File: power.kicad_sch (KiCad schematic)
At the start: 32 parts, among them J1 Barrel_Jack_MountingPin, J2 Conn_02x04_Odd_Even, J3 Conn_02x04_Odd_Even, Q1 SI2301CDS-T1-GE3, SW1 Power, U2 TPS54302

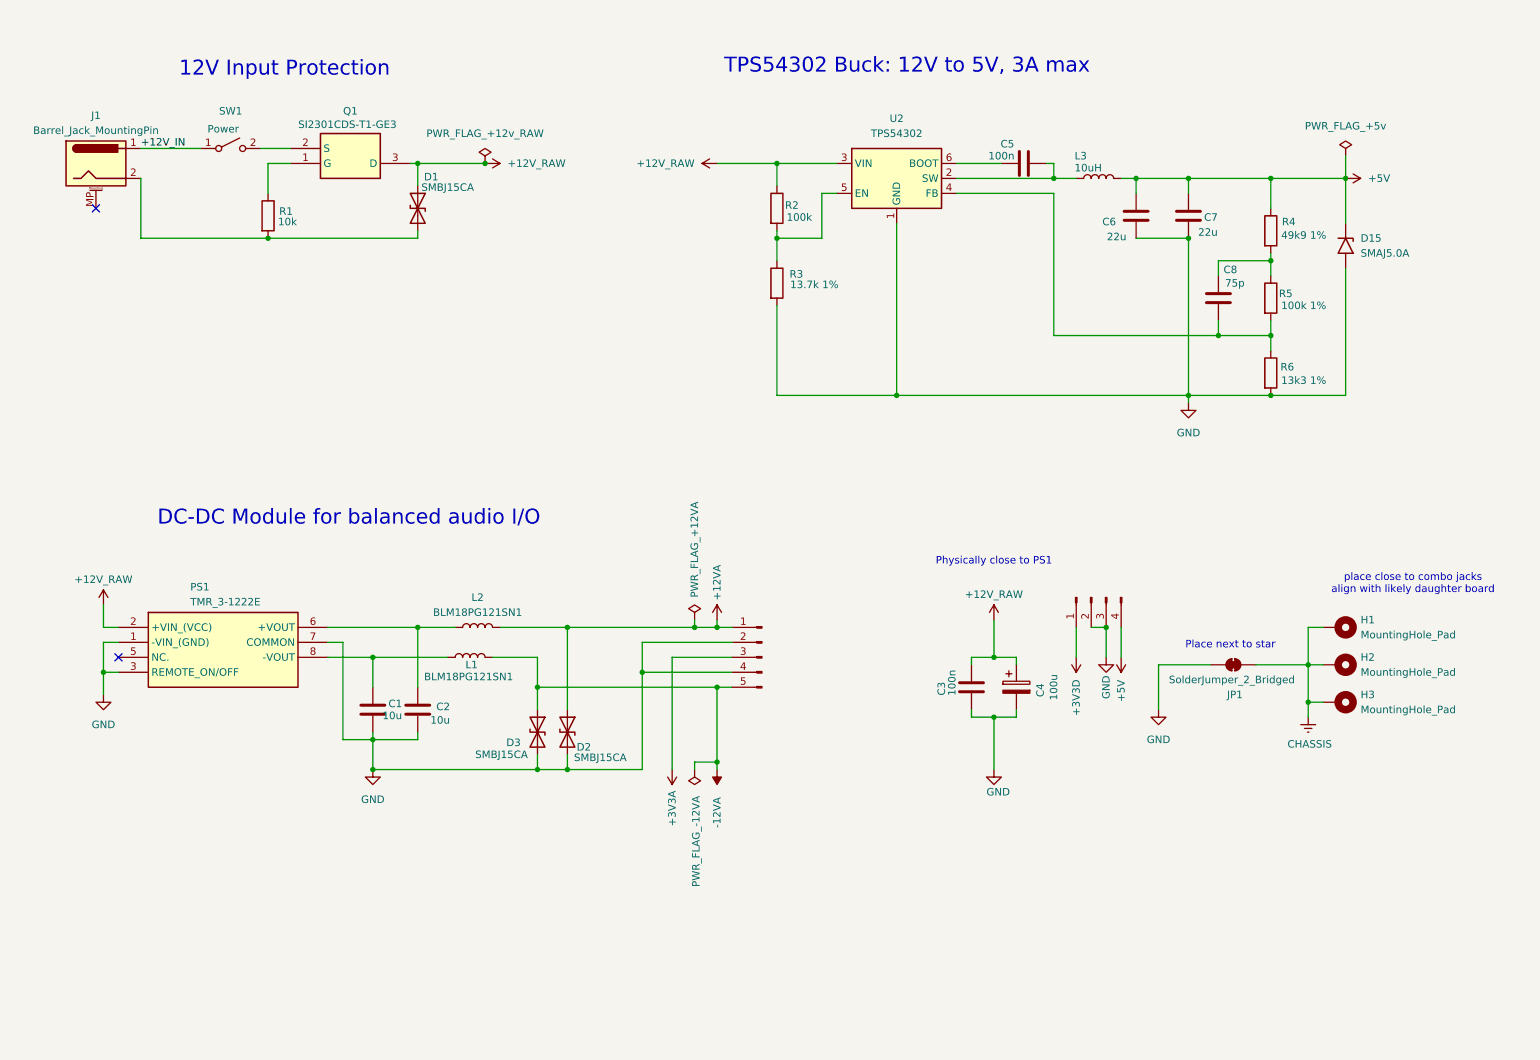
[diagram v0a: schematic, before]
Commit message: change docs to use RS3-1212D
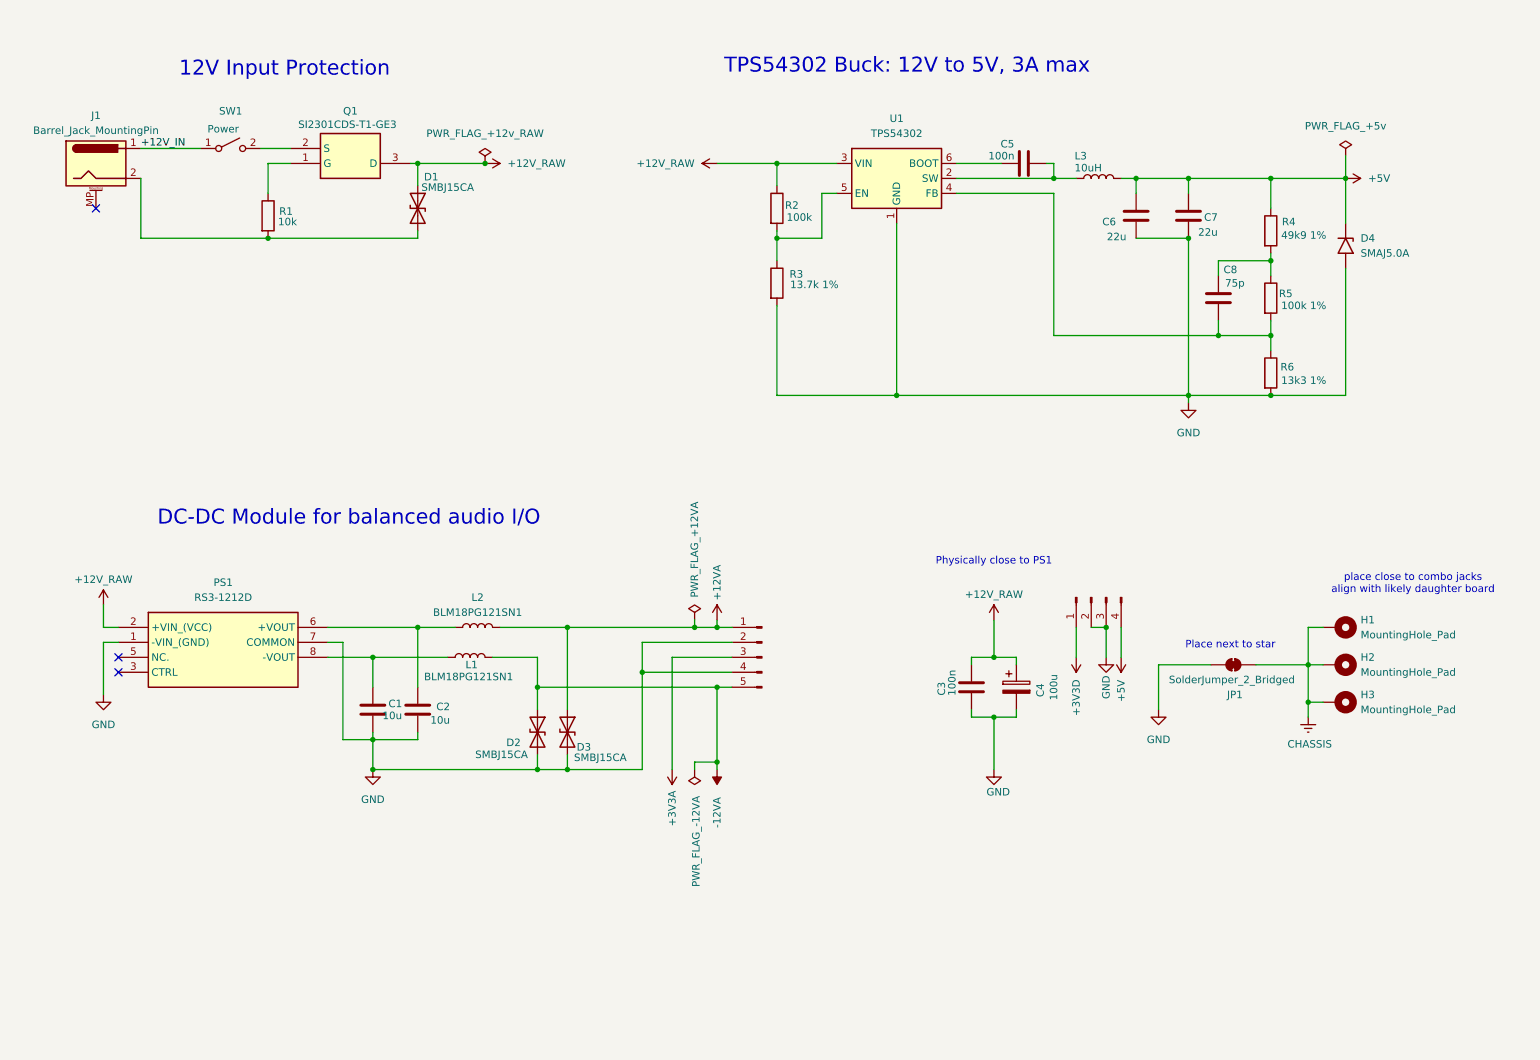
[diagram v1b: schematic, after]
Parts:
- removed PS1: TMR_3-1222E, daisy-studio:TMR1210, symbol daisy-studio:TMR_3-1222E
- added PS1: RS3-1212D, daisy-studio:TMR1210, symbol daisy-studio:RS3-1212D
- renumbered D3 to D2, D2 to D3, D15 to D4, U2 to U1
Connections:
- net +12V_RAW: now also PS1.2 (+VIN_(VCC))
- net GND: now also PS1.1 (-VIN_(GND)), PS1.7 (COMMON)
- net at C2.1, L2.1: now also PS1.6 (+VOUT)
- net at C1.1, L1.1: now also PS1.8 (-VOUT)
- no-connect marks 2 -> 3

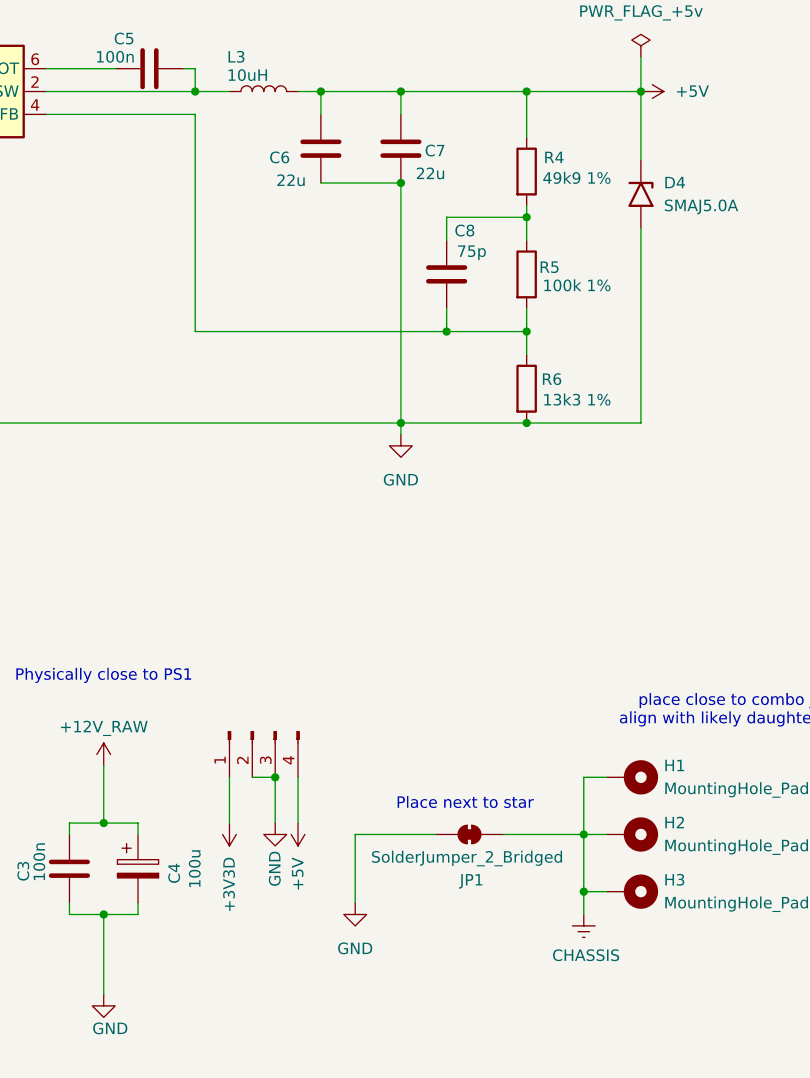
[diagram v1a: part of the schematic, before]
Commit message: clean up symbols and values
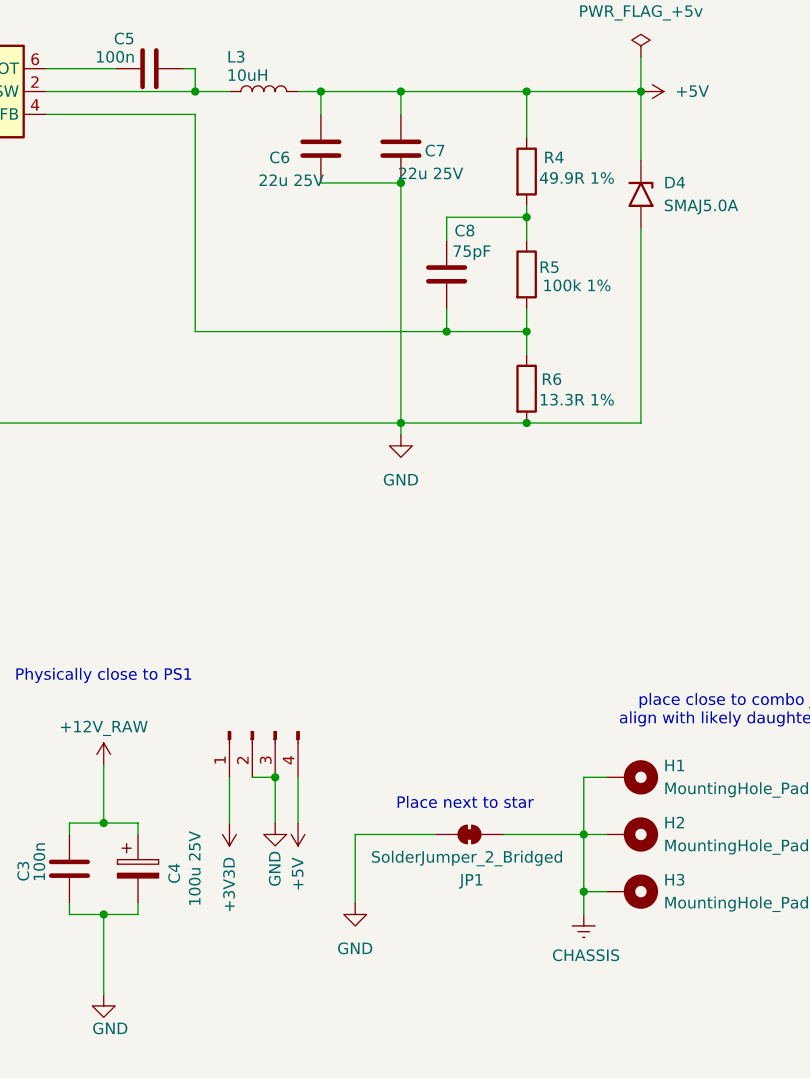
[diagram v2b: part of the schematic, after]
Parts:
- C4: value 100u -> 100u 25V
- C6, C7: value 22u -> 22u 25V
- C8: value 75p -> 75pF
- R4: value 49k9 1% -> 49.9R 1%
- R6: value 13k3 1% -> 13.3R 1%
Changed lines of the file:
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@@
 			)
 		)
-		(property "Value" "75p"
+		(property "Value" "75pF"
 			(at 218.694 69.85 0)
 			(effects
@@
 			)
 		)
-		(property "Value" "49k9 1%"
+		(property "Value" "49.9R 1%"
 			(at 230.378 61.722 0)
 			(effects
@@
 			)
 		)
-		(property "Value" "22u"
+		(property "Value" "22u 25V"
 			(at 214.122 61.214 0)
 			(effects
@@
 			)
 		)
-		(property "Value" "100u"
+		(property "Value" "100u 25V"
 			(at 187.96 138.43 90)
 			(effects
@@
 			)
 		)
-		(property "Value" "13k3 1%"
+		(property "Value" "13.3R 1%"
 			(at 230.378 86.36 0)
 			(effects
@@
 			)
 		)
-		(property "Value" "22u"
+		(property "Value" "22u 25V"
 			(at 198.628 61.976 0)
 			(effects

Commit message: Fix R6
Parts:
- R6: value 13.3R 1% -> 13.3K 1%
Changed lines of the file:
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@@
 			)
 		)
-		(property "Value" "13.3R 1%"
+		(property "Value" "13.3K 1%"
 			(at 230.378 86.36 0)
 			(effects

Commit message: lots of pcb work
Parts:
- J2: value Conn_02x04_Odd_Even -> ~; footprint Connector_PinHeader_2.54mm:PinHeader_2x04_P2.54mm_Vertical -> Connector_PinHeader_2.54mm:PinHeader_2x03_P2.54mm_Vertical; symbol Connector:Conn_01x05_Pin -> Connector:Conn_01x06_Pin
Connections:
- net GND: now also J2.6 (Pin_6)
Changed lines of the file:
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@@
 	(wire
 		(pts
-			(xy 130.81 128.27) (xy 133.35 128.27)
+			(xy 130.81 128.27) (xy 134.62 128.27)
 		)
 		(stroke
@@
 	(wire
 		(pts
-			(xy 118.11 135.89) (xy 133.35 135.89)
+			(xy 118.11 135.89) (xy 134.62 135.89)
 		)
 		(stroke
@@
 	(wire
 		(pts
-			(xy 133.35 133.35) (xy 123.19 133.35)
+			(xy 134.62 133.35) (xy 123.19 133.35)
 		)
 		(stroke
@@
 	(wire
 		(pts
+			(xy 134.62 140.97) (xy 134.62 152.4)
+		)
+		(stroke
+			(width 0)
+			(type default)
+		)
+	)
+	(wire
+		(pts
 			(xy 210.82 52.07) (xy 201.93 52.07)
 		)
@@
 	(wire
 		(pts
-			(xy 133.35 130.81) (xy 118.11 130.81)
+			(xy 134.62 130.81) (xy 118.11 130.81)
 		)
 		(stroke
@@
 	(wire
 		(pts
-			(xy 130.81 138.43) (xy 133.35 138.43)
+			(xy 130.81 138.43) (xy 134.62 138.43)
 		)
 		(stroke
@@
 	)
 	(symbol
-		(lib_id "Connector:Conn_01x05_Pin")
-		(at 138.43 133.35 0)
+		(lib_id "Connector:Conn_01x06_Pin")
+		(at 139.7 133.35 0)
 		(mirror y)
 		(unit 1)
@@
 		(dnp no)
 		(property "Reference" "J2"
-			(at 137.922 141.224 90)
+			(at 139.192 141.224 90)
 			(effects
 				(font
@@
 			)
 		)
-		(property "Value" "Conn_02x04_Odd_Even"
-			(at 136.144 143.002 90)
+		(property "Value" "~"
+			(at 137.414 143.002 90)
 			(effects
 				(font
@@
 			)
 		)
-		(property "Footprint" "Connector_PinHeader_2.54mm:PinHeader_2x04_P2.54mm_Vertical"
-			(at 138.43 133.35 0)
+		(property "Footprint" "Connector_PinHeader_2.54mm:PinHeader_2x03_P2.54mm_Vertical"
+			(at 139.7 133.35 0)
 			(effects
 				(font
@@
 		)
 		(property "Datasheet" "~"
-			(at 138.43 133.35 0)
+			(at 139.7 133.35 0)
 			(effects
 				(font
@@
 			)
 		)
-		(property "Description" "Generic connector, single row, 01x05, script generated"
-			(at 138.43 133.35 0)
+		(property "Description" "Generic connector, single row, 01x06, script generated"
+			(at 139.7 133.35 0)
 			(effects
 				(font
@@
 		(pin "5"
 		)
+		(pin "6"
+		)
 		(instances
 			(project "daisy-studio"
@@
 		(on_board yes)
 		(dnp no)
-		(property "Reference" "#PWR09"
+		(property "Reference" "#PWR010"
 			(at 177.8 130.81 0)
 			(effects
@@
 			(project "daisy-studio"
 				(path "/55cca6a8-30da-4c13-b2f2-a01401e2b54c/a1b2c3d4-1111-4000-8000-000000000001"
-					(reference "#PWR09")
+					(reference "#PWR010")
 					(unit 1)
 				)
@@
 		(on_board yes)
 		(dnp no)
-		(property "Reference" "#PWR010"
+		(property "Reference" "#PWR011"
 			(at 177.8 158.75 0)
 			(effects
@@
 			(project "triptech"
 				(path "/55cca6a8-30da-4c13-b2f2-a01401e2b54c/a1b2c3d4-1111-4000-8000-000000000001"
-					(reference "#PWR010")
+					(reference "#PWR011")
 					(unit 1)
 				)
@@
 		(dnp no)
 		(fields_autoplaced yes)
-		(property "Reference" "#PWR014"
+		(property "Reference" "#PWR015"
 			(at 205.74 148.59 0)
 			(effects
@@
 			(project "daisy-studio"
 				(path "/55cca6a8-30da-4c13-b2f2-a01401e2b54c/a1b2c3d4-1111-4000-8000-000000000001"
-					(reference "#PWR014")
+					(reference "#PWR015")
 					(unit 1)
 				)
@@
 	(symbol
 		(lib_id "power:GND")
+		(at 134.62 152.4 0)
+		(unit 1)
+		(exclude_from_sim no)
+		(in_bom yes)
+		(on_board yes)
+		(dnp no)
+		(property "Reference" "#PWR09"
+			(at 134.62 158.75 0)
+			(effects
+				(font
+					(size 1.27 1.27)
+				)
+				(hide yes)
+			)
+		)
+		(property "Value" "GND"
+			(at 134.62 157.48 90)
+			(effects
+				(font
+					(size 1.27 1.27)
+				)
+			)
+		)
+		(property "Footprint" ""
+			(at 134.62 152.4 0)
+			(effects
+				(font
+					(size 1.27 1.27)
+				)
+				(hide yes)
+			)
+		)
+		(property "Datasheet" ""
+			(at 134.62 152.4 0)
+			(effects
+				(font
+					(size 1.27 1.27)
+				)
+				(hide yes)
+			)
+		)
+		(property "Description" "Power symbol creates a global label with name \"GND\" , ground"
+			(at 134.62 152.4 0)
+			(effects
+				(font
+					(size 1.27 1.27)
+				)
+				(hide yes)
+			)
+		)
+		(pin "1"
+		)
+		(instances
+			(project "daisy-studio"
+				(path "/55cca6a8-30da-4c13-b2f2-a01401e2b54c/a1b2c3d4-1111-4000-8000-000000000001"
+					(reference "#PWR09")
+					(unit 1)
+				)
+			)
+		)
+	)
+	(symbol
+		(lib_id "power:GND")
 		(at 26.67 139.7 0)
 		(unit 1)
@@
 		(on_board yes)
 		(dnp no)
-		(property "Reference" "#PWR011"
+		(property "Reference" "#PWR012"
 			(at 191.77 129.54 0)
 			(effects
@@
 			(project "daisy-studio"
 				(path "/55cca6a8-30da-4c13-b2f2-a01401e2b54c/a1b2c3d4-1111-4000-8000-000000000001"
-					(reference "#PWR011")
+					(reference "#PWR012")
 					(unit 1)
 				)
@@
 		(on_board yes)
 		(dnp no)
-		(property "Reference" "#PWR016"
+		(property "Reference" "#PWR017"
 			(at 231.14 149.86 0)
 			(effects
@@
 			(project "daisy-studio"
 				(path "/55cca6a8-30da-4c13-b2f2-a01401e2b54c/a1b2c3d4-1111-4000-8000-000000000001"
-					(reference "#PWR016")
+					(reference "#PWR017")
 					(unit 1)
 				)
@@
 		(dnp no)
 		(fields_autoplaced yes)
-		(property "Reference" "#PWR015"
+		(property "Reference" "#PWR016"
 			(at 210.82 96.52 0)
 			(effects
@@
 			(project "triptech"
 				(path "/55cca6a8-30da-4c13-b2f2-a01401e2b54c/a1b2c3d4-1111-4000-8000-000000000001"
-					(reference "#PWR015")
+					(reference "#PWR016")
 					(unit 1)
 				)
@@
 		(on_board yes)
 		(dnp no)
-		(property "Reference" "#PWR012"
+		(property "Reference" "#PWR013"
 			(at 196.85 139.7 0)
 			(effects
@@
 			(project "daisy-studio"
 				(path "/55cca6a8-30da-4c13-b2f2-a01401e2b54c/a1b2c3d4-1111-4000-8000-000000000001"
-					(reference "#PWR012")
+					(reference "#PWR013")
 					(unit 1)
 				)
@@
 		(dnp no)
 		(fields_autoplaced yes)
-		(property "Reference" "#PWR017"
+		(property "Reference" "#PWR018"
 			(at 233.68 52.07 0)
 			(effects
@@
 			(project ""
 				(path "/55cca6a8-30da-4c13-b2f2-a01401e2b54c/a1b2c3d4-1111-4000-8000-000000000001"
-					(reference "#PWR017")
+					(reference "#PWR018")
 					(unit 1)
 				)
@@
 		(on_board yes)
 		(dnp no)
-		(property "Reference" "#PWR013"
+		(property "Reference" "#PWR014"
 			(at 199.39 129.54 0)
 			(effects
@@
 			(project "daisy-studio"
 				(path "/55cca6a8-30da-4c13-b2f2-a01401e2b54c/a1b2c3d4-1111-4000-8000-000000000001"
-					(reference "#PWR013")
+					(reference "#PWR014")
 					(unit 1)
 				)
